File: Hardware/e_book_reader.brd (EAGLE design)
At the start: 170.2 x 111.2 mm, 103 parts

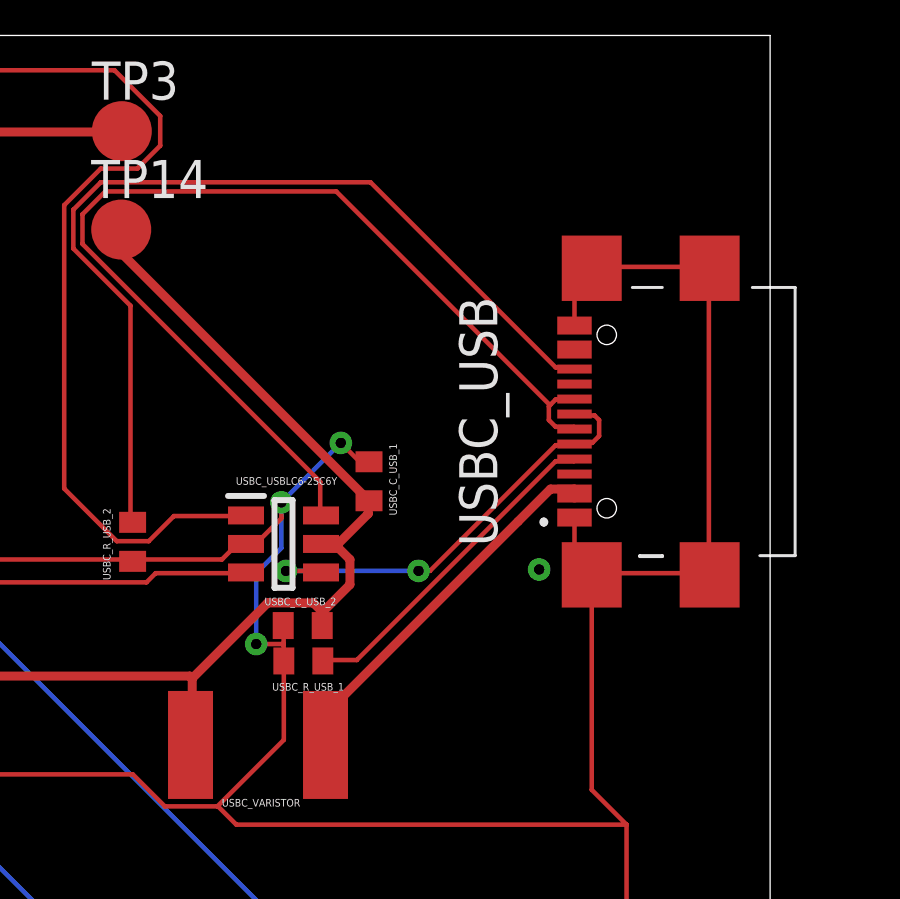
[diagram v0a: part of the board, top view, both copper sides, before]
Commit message: Fixed issue #1 by fixing VUSB connection
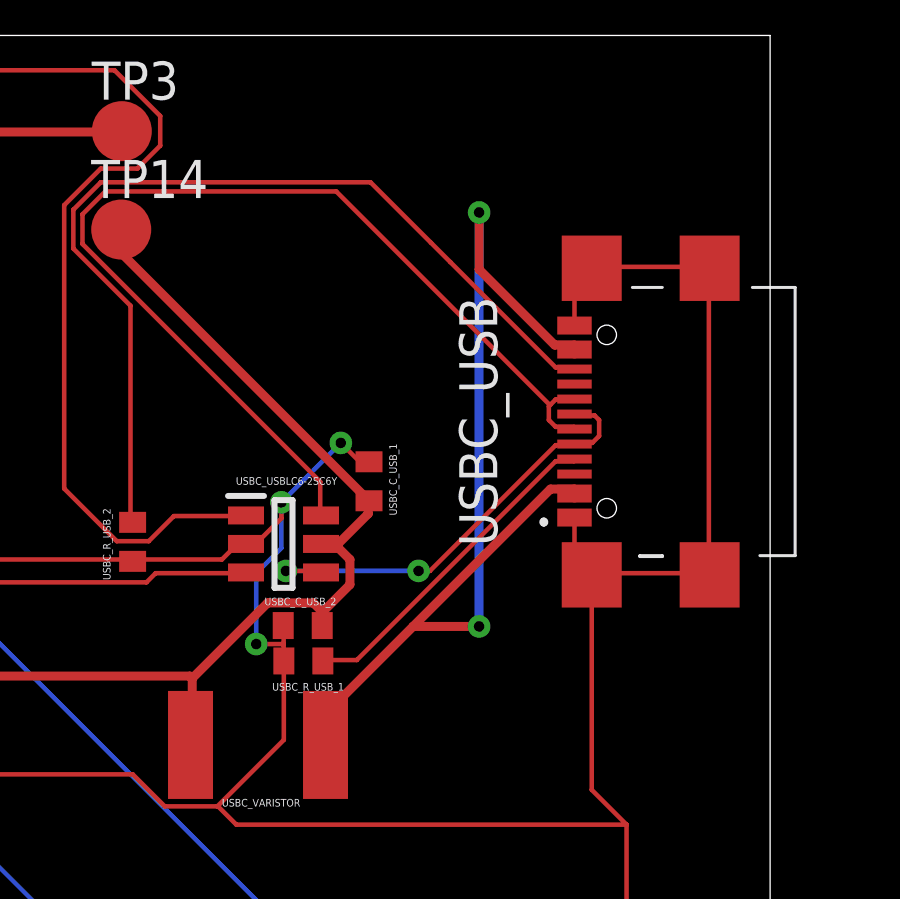
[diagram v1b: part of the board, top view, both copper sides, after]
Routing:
- net VUSB: track 12.7 -> 35.2 mm, vias 0 -> 2
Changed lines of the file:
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@@
 <wire x1="62.7888" y1="6.7056" x2="61.8744" y2="5.7912" width="0.1524" layer="1"/>
 <wire x1="71.7804" y1="6.7056" x2="62.7888" y2="6.7056" width="0.1524" layer="1"/>
-<wire x1="77.9526" y1="0.5334" x2="71.7804" y2="6.7056" width="0.1524" layer="1"/>
+<wire x1="77.9526" y1="0.5334" x2="74.443" y2="4.043" width="0.1524" layer="1"/>
+<wire x1="74.443" y1="4.043" x2="73.793" y2="4.693" width="0.1524" layer="1"/>
+<wire x1="73.793" y1="4.693" x2="71.7804" y2="6.7056" width="0.1524" layer="1"/>
 <wire x1="78.5622" y1="0.5334" x2="77.9526" y2="0.5334" width="0.1524" layer="1"/>
 <wire x1="63.7794" y1="-4.572" x2="63.85" y2="-4.63" width="0.1524" layer="1"/>
@@
 <wire x1="78.6384" y1="-1.0668" x2="79.248" y2="-1.0668" width="0.1524" layer="1"/>
 <wire x1="78.6384" y1="-1.9812" x2="78.579" y2="-2.02" width="0.1524" layer="1"/>
-<wire x1="78.6384" y1="-1.0668" x2="78.579" y2="-1.02" width="0.1524" layer="1"/>
+<wire x1="78.579" y1="-1.02" x2="78.6384" y2="-1.0668" width="0.1524" layer="1"/>
 <wire x1="68.961" y1="-6.2484" x2="70.104" y2="-6.2484" width="0.1524" layer="1"/>
 <wire x1="73.3806" y1="-6.2484" x2="68.961" y2="-6.2484" width="0.1524" layer="16"/>
@@
 <wire x1="78.579" y1="-3.82" x2="78.579" y2="-3.52" width="0.3" layer="1"/>
 <wire x1="78.579" y1="-3.52" x2="77.78" y2="-3.52" width="0.3" layer="1"/>
-<wire x1="77.78" y1="-3.52" x2="76.7" y2="-4.6" width="0.3" layer="1"/>
-<wire x1="76.7" y1="-4.6" x2="70.28" y2="-11.02" width="0.3" layer="1"/>
+<wire x1="77.78" y1="-3.52" x2="73.2" y2="-8.1" width="0.3" layer="1"/>
+<wire x1="73.2" y1="-8.1" x2="70.28" y2="-11.02" width="0.3" layer="1"/>
 <wire x1="70.28" y1="-11.02" x2="70.28" y2="-12.05" width="0.3" layer="1"/>
-<wire x1="78.579" y1="0.98" x2="78.579" y2="1.28" width="0" layer="19" extent="1-1"/>
-<wire x1="78.579" y1="-3.52" x2="78.579" y2="0.98" width="0" layer="19" extent="1-1"/>
+<via x="75.4" y="-8.1" extent="1-16" drill="0.35" alwaysstop="yes">
+</via>
+<wire x1="75.4" y1="-8.1" x2="73.2" y2="-8.1" width="0.3" layer="1"/>
+<via x="75.4" y="5.7" extent="1-16" drill="0.35" alwaysstop="yes">
+</via>
+<wire x1="78.579" y1="1.28" x2="77.92" y2="1.28" width="0.3" layer="1"/>
+<wire x1="77.92" y1="1.28" x2="75.4" y2="3.8" width="0.3" layer="1"/>
+<wire x1="75.4" y1="3.8" x2="75.4" y2="5.7" width="0.3" layer="1"/>
+<wire x1="78.579" y1="0.98" x2="78.579" y2="1.28" width="0.3" layer="1"/>
+<wire x1="75.4" y1="5.7" x2="75.4" y2="-8.1" width="0.3" layer="16"/>
 </signal>
 <signal name="SRC" class="1">
@@
 <wire x1="6.096" y1="-34.671" x2="6.12" y2="-34.65" width="0.1524" layer="1"/>
 </signal>
-<signal name="N$10">
-<via x="77.4" y="-6.2" extent="1-16" drill="0.35" alwaysstop="yes">
-</via>
-</signal>
 <signal name="N$12">
